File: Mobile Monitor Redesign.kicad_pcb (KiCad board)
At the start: 4 copper layers, 49 x 39.1 mm, 98 parts, among them J1 Conn_01x02_Pin, J2 Conn_01x08_Pin, J3 Conn_01x08_Pin, J4 USB_C_Receptacle_USB2.0_16P, J5 Conn_02x03_Odd_Even, J6 Micro_SD_Card_Det1, J7 Conn_01x05_Pin, J8 Conn_01x06_Socket, Q1 2N7002, Q2 AO3401A, Q5 AO3401A, Q6 2N7002, SW1 SW_Push, U1 ATmega2560-16A, U10 BQ27441DRZR-G1A, U11 TPL5010, U2 DS3232M, U5 XL4005, U6 IP5306, U7 CH340C, U8 FP6298XR, U9 AMS1117-3.3, Y1 Crystal

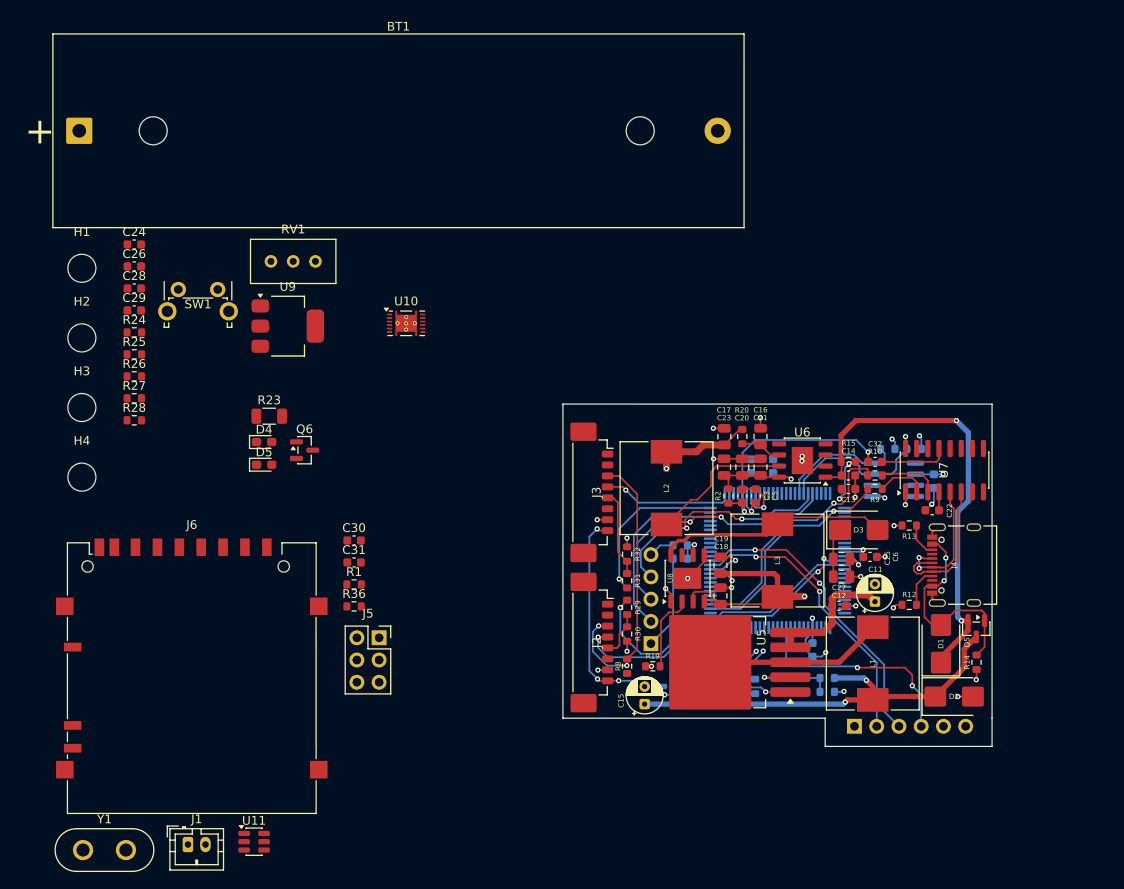
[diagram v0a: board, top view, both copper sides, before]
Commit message: cleaned up more routing and component placement
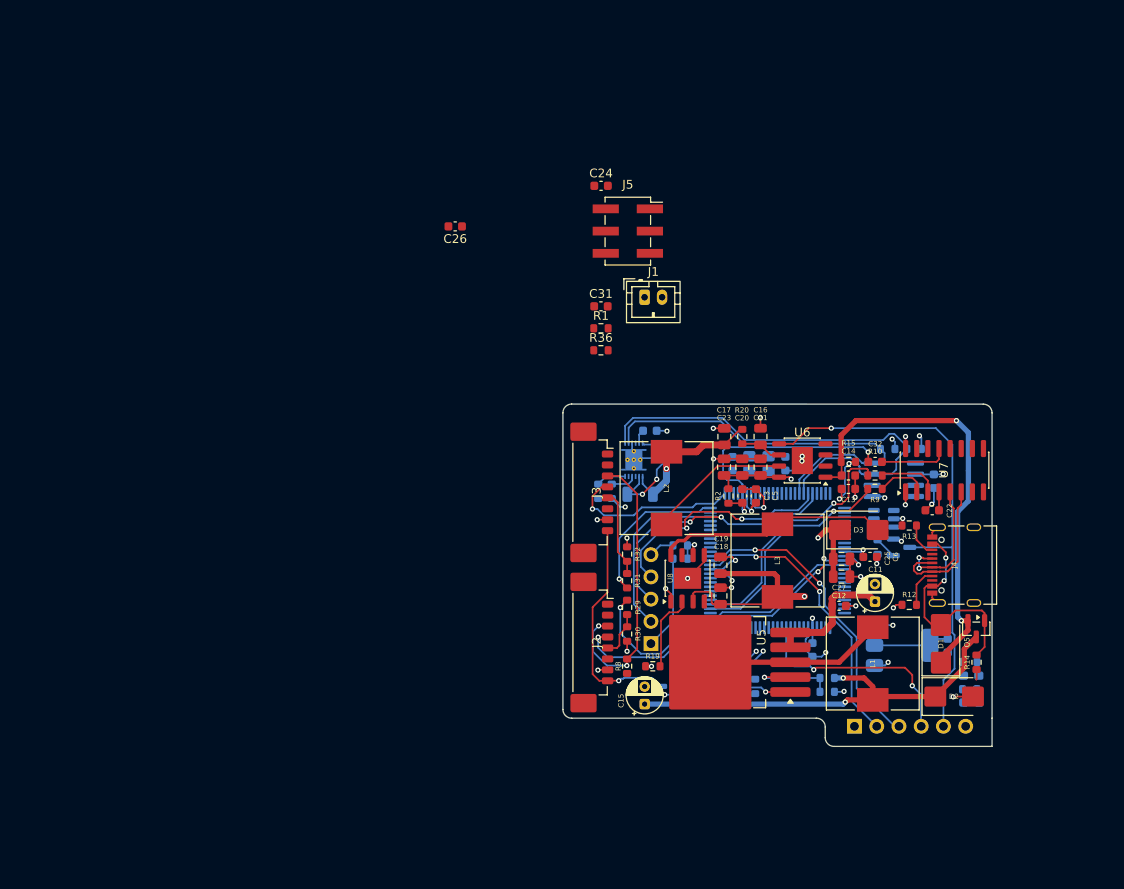
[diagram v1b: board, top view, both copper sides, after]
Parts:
- removed BT1: Battery_Cell, Battery:BatteryHolder_MPD_BH-18650-PC
- removed H1, H2, H3, H4: MountingHole, MountingHole:MountingHole_3.2mm_M3
- removed J6: Micro_SD_Card_Det1, Connector_Card:SD_Hirose_DM1AA_SF_PEJ82
- removed RV1: R_Potentiometer_Trim, Potentiometer_THT:Potentiometer_Bourns_3296W_Vertical
- removed SW1: SW_Push, Button_Switch_THT:SW_Tactile_SPST_Angled_PTS645Vx58-2LFS
- C28, C29, C30, D4, D5, Q6, R23, R24, R25, R26, R27, R28, U10, U11, U9: moved to B.Cu
- J5: footprint Connector_PinSocket_2.54mm:PinSocket_2x03_P2.54mm_Vertical -> Connector_PinSocket_2.54mm:PinSocket_2x03_P2.54mm_Vertical_SMD
- Y1: footprint Crystal:Crystal_HC50_Vertical -> Crystal:Crystal_SMD_3225-4Pin_3.2x2.5mm; moved to B.Cu
- moved R28 100.2 mm to (163.3, 113.8), turned to 180 degrees
- moved R27 100.1 mm to (163.3, 110.7)
- moved Y1 88.9 mm to (139.2, 88.0)
- moved R25 87.7 mm to (152.8, 97.5), turned to 90 degrees
- moved D5 85.2 mm to (163.5, 115.3), turned to 180 degrees
- moved D4 85.0 mm to (163.5, 112.2), turned to 180 degrees
- moved J1 81.4 mm to (126.2, 69.0)
- moved U11 80.8 mm to (153.5, 94.3), turned to 180 degrees
- moved U9 79.1 mm to (155.6, 108.8)
- moved Q6 69.1 mm to (155.5, 97.6)
- moved C30 68.8 mm to (160.8, 108.8), turned to -90 degrees
- moved C28 62.5 mm to (127.5, 86.6), turned to -90 degrees
- moved C29 60.5 mm to (126.8, 84.3)
- moved R24 57.5 mm to (122.4, 91.2), turned to 90 degrees
- moved R26 54.6 mm to (120.9, 91.2), turned to 90 degrees
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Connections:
- J8 pad 5: unconnected-(J8-Pin_5-Pad5) -> PWR_SWITCH
- R27 pad 2: status_led -> VIN
- R28 pad 1: VIN -> status_led
- U1 pad 71: unconnected-(U1-PA7-Pad71) -> status_led
- U10 pad 1: /power/SDA -> SDA
- U10 pad 2: /power/SCL -> SCL
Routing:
- net PWR_SWITCH: track 0.00 -> 59.0 mm, vias 0 -> 1
- net SDA: track 17.3 -> 54.1 mm
- net SCL: track 14.5 -> 46.7 mm
- net ADJUSTABLE_GSM_PWR_4.2: track 16.4 -> 47.4 mm, vias 0 -> 1
- net GND: track 81.0 -> 95.0 mm, vias 31 -> 34
- net /power/BATTERY_PRIMARY: track 0.00 -> 13.5 mm, vias 0 -> 2
- net +3.3V: track 0.00 -> 8.66 mm
- net /power/BATTERY_SEC: track 62.7 -> 68.8 mm
- net SOFT_PWR_SWITCH: track 0.00 -> 5.79 mm
- net PMS_RX: track 15.0 -> 20.1 mm
- net Net-(U10-GPOUT): track 0.00 -> 3.43 mm
- net RESET: track 26.2 -> 29.5 mm
- net Net-(U10-BIN): track 0.00 -> 2.95 mm
- net +5V: track 41.5 -> 43.6 mm, vias 11 -> 12
- net Net-(U10-V_{DD}): track 0.00 -> 1.54 mm
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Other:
- outline, holes or cut-outs redrawn

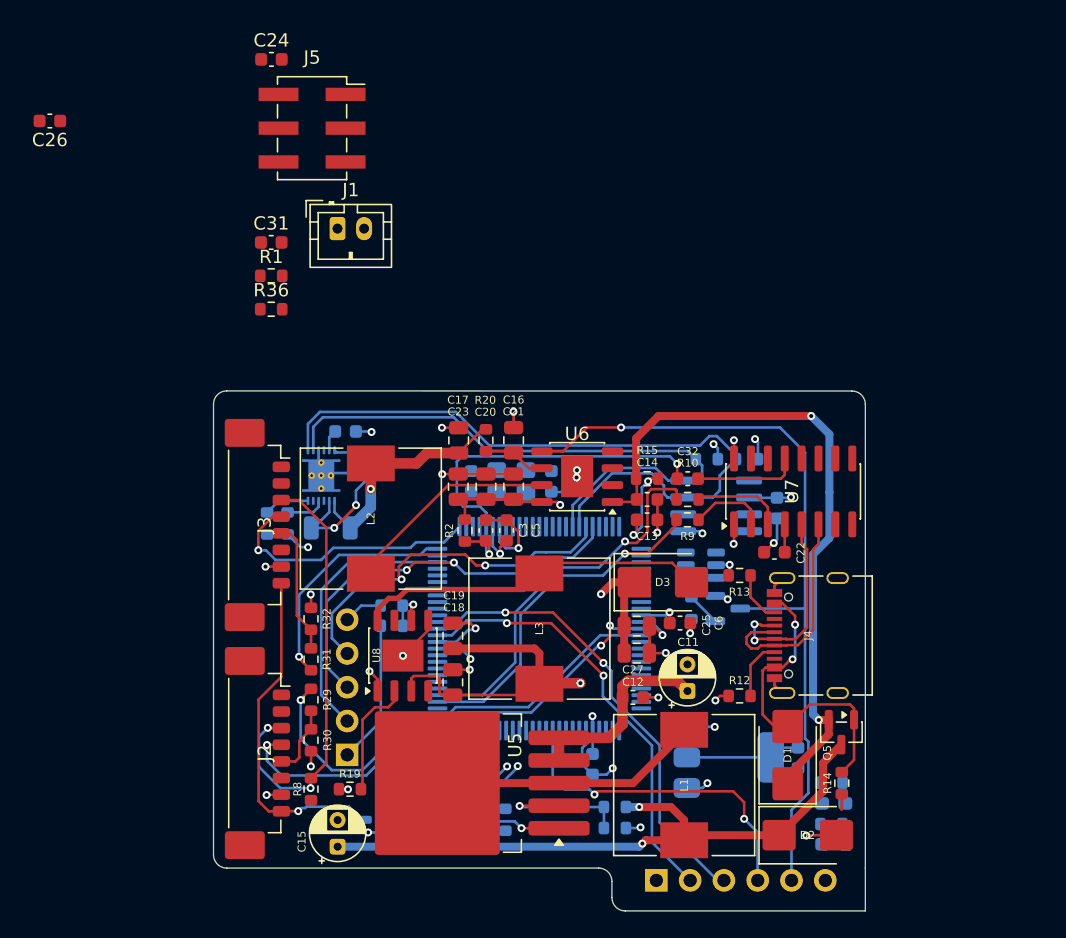
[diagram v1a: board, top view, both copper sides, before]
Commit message: routed the l80 gps daughter board and a few more modifications
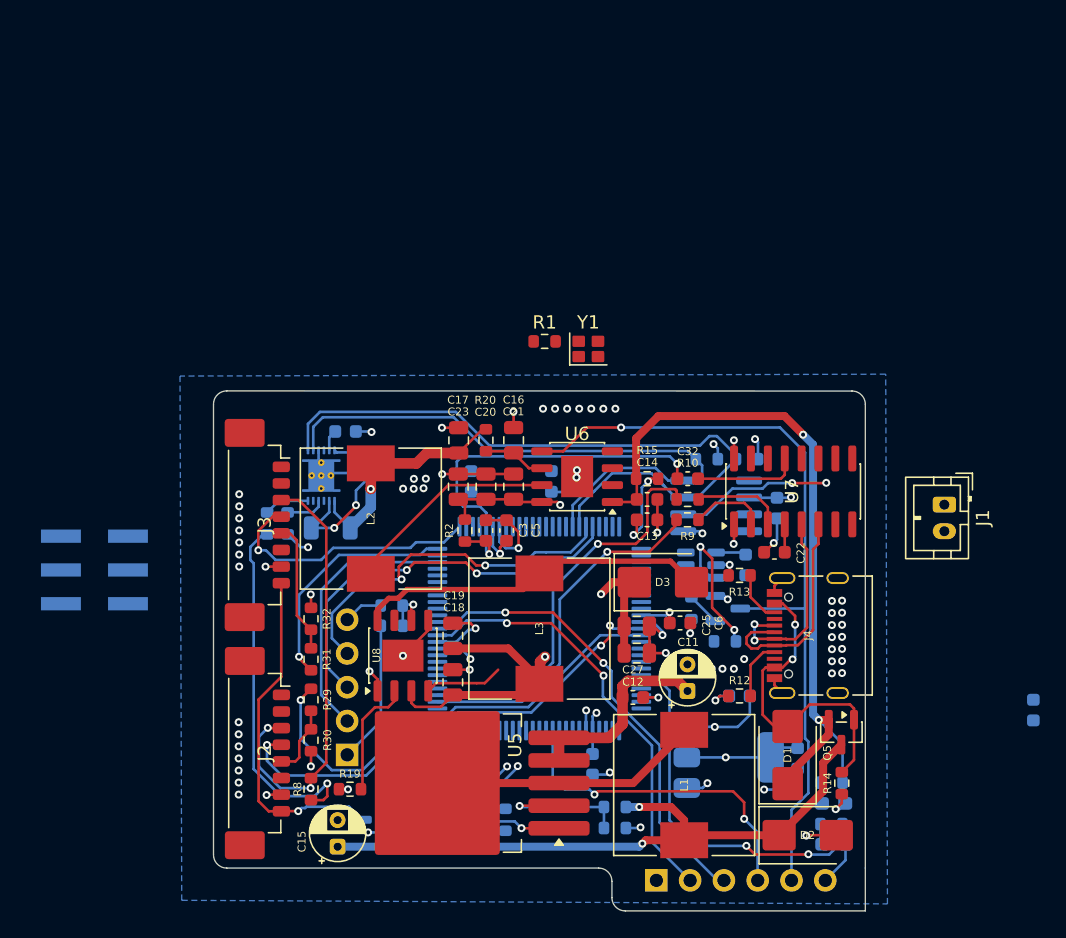
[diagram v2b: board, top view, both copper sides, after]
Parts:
- C24, C26, C31, J5, R36: moved to B.Cu
- Y1: value Crystal -> Crystal_GND23; footprint Crystal:Crystal_SMD_3225-4Pin_3.2x2.5mm -> Crystal:Crystal_SMD_SeikoEpson_FA128-4Pin_2.0x1.6mm; moved to F.Cu
- moved C26 73.9 mm to (160.8, 108.8), turned to -90 degrees
- moved C24 59.4 mm to (156.4, 104.1), turned to 180 degrees
- moved J1 50.1 mm to (171.8, 89.8), turned to -90 degrees
- moved C31 43.1 mm to (156.8, 94.3), turned to -90 degrees
- moved R36 42.3 mm to (155.3, 100.0)
- moved J5 37.0 mm to (107.9, 94.7), turned to 180 degrees
- moved R1 21.1 mm to (141.7, 77.5)
- moved C30 18.1 mm to (178.5, 105.2)
- moved Y1 11.5 mm to (145.0, 78.1)
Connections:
- Y1 pad 1: Net-(U1-XTAL2) -> Net-(U1-XTAL1)
- Y1 pad 2: Net-(U1-XTAL1) -> GND
- Y1 pad 3: (no net) -> GND
- Y1 pad 4: (no net) -> Net-(U1-XTAL2)
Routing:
- net +3.3V: track 8.66 -> 67.9 mm, vias 0 -> 2
- net status_led: track 0.00 -> 27.9 mm, vias 0 -> 2
- net VBAT_RTC: track 0.00 -> 11.7 mm, vias 0 -> 2
- net Net-(U11-DELAY/M_RST): track 0.00 -> 11.4 mm, vias 0 -> 2
- net GND: track 95.0 -> 101.5 mm, vias 34 -> 81
- net GSM_PWR_EN: track 0.00 -> 5.92 mm
- net +5V: track 43.6 -> 48.4 mm
- net /power/BATTERY_SEC: track 68.8 -> 64.7 mm
- net VIN: track 51.3 -> 54.6 mm
- net /BATTERY_SEC: track 0.00 -> 2.29 mm
- net ADJUSTABLE_GSM_PWR_4.2: track 47.4 -> 45.3 mm
- net Net-(D4-A): track 0.00 -> 1.60 mm
- net Net-(D5-A): track 0.00 -> 1.58 mm
- net TXD0: track 29.1 -> 30.1 mm
- net RXD0: track 26.1 -> 26.7 mm
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- added copper zone on B.Cu, net GND

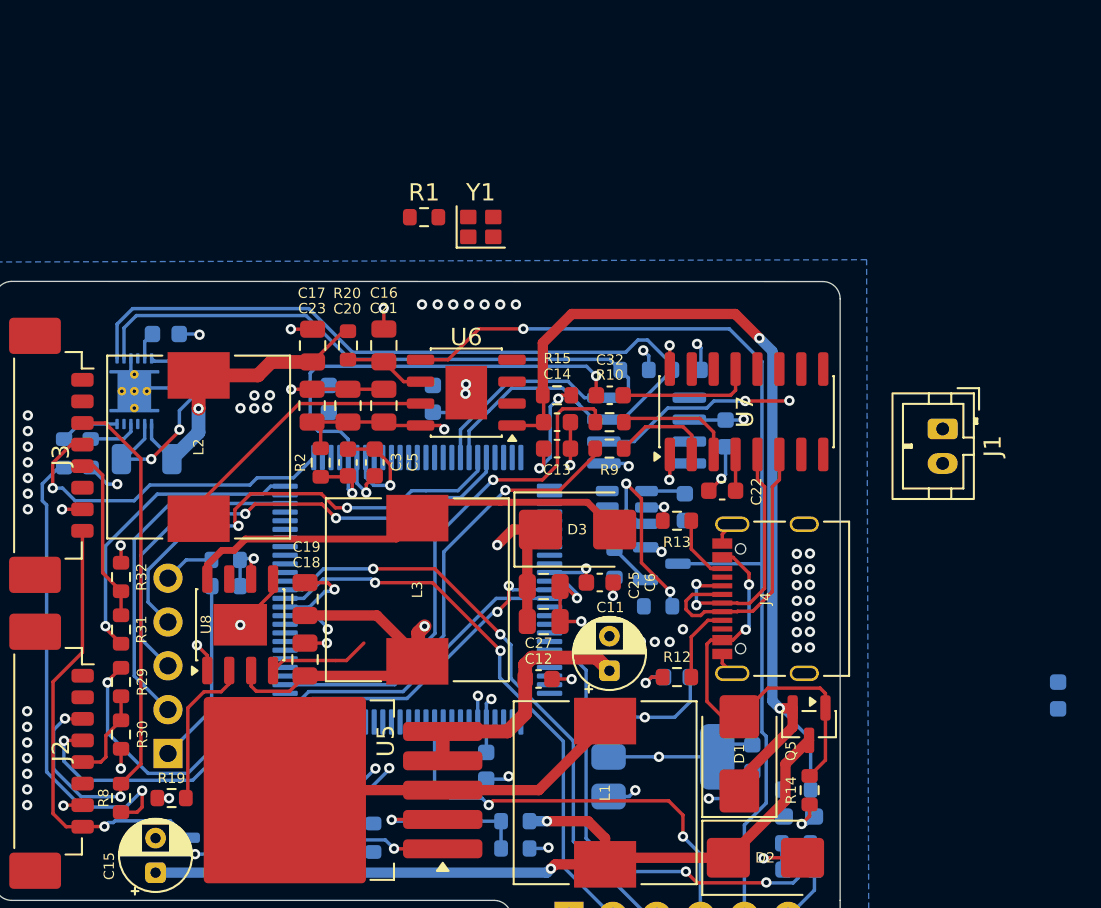
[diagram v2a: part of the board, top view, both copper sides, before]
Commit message: updated routing and placement of devices on both PCBS
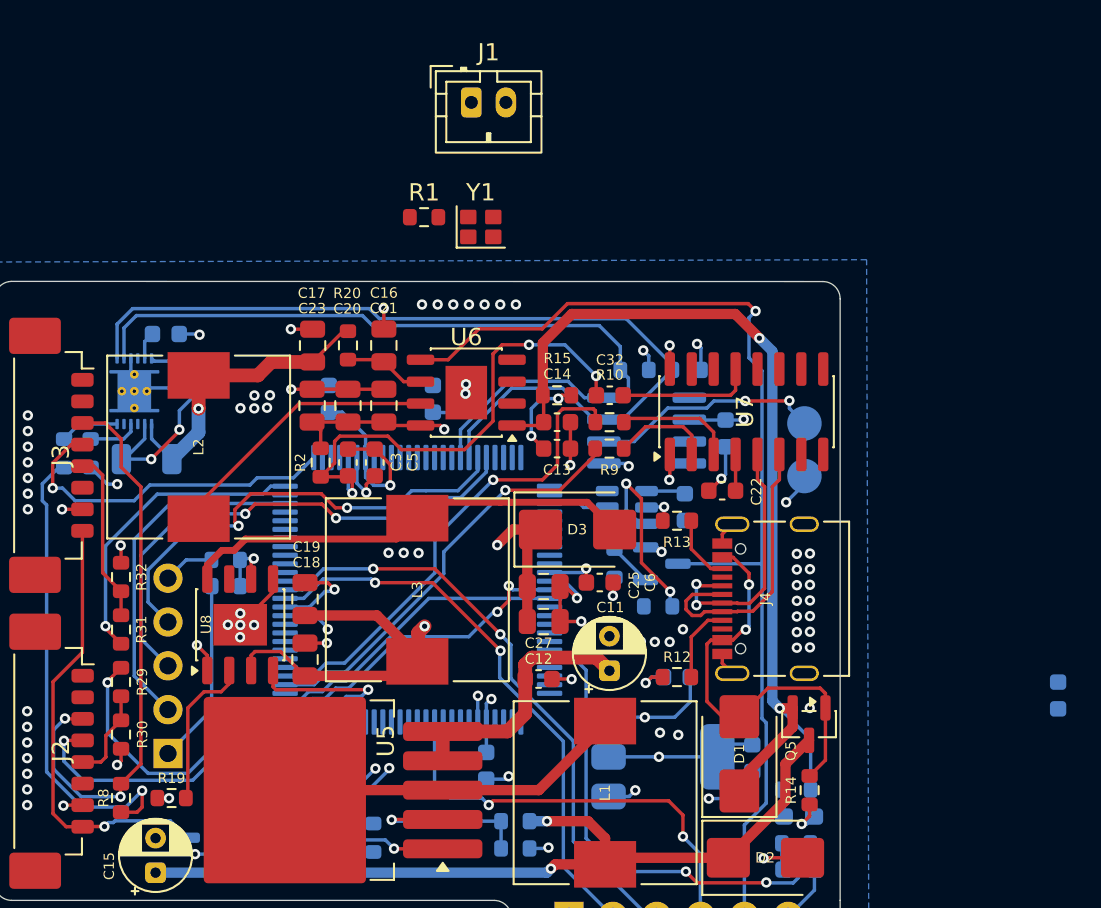
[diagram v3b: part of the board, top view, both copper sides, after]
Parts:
- added REF**: TestPoint_Pad_D2.0mm, TestPoint:TestPoint_Pad_D2.0mm, B.Cu at (163.8, 89.4)
- added REF**: TestPoint_Pad_D2.0mm, TestPoint:TestPoint_Pad_D2.0mm, B.Cu at (163.8, 92.5)
- moved J1 33.2 mm to (144.5, 70.8), turned to 0 degrees
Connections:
- U1 pad 53: unconnected-(U1-PC0-Pad53) -> SOFT_PWR_SWITCH
- U1 pad 97: unconnected-(U1-PF0-Pad97) -> GSM_PWR_EN
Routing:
- net GND: track 101.5 -> 107.3 mm, vias 81 -> 92
- net GSM_PWR_EN: track 5.92 -> 9.59 mm, vias 0 -> 1
- net SOFT_PWR_SWITCH: track 5.79 -> 9.23 mm
- net PWR_SWITCH: track 59.0 -> 62.0 mm
- net RXD0: track 26.7 -> 24.6 mm
- net TXD0: track 30.1 -> 28.0 mm
- net VBAT_RTC: track 11.7 -> 13.4 mm
- net Net-(C13-Pad1): track 6.57 -> 5.25 mm
- net SDA: track 53.5 -> 52.5 mm
- net SCL: track 46.7 -> 47.5 mm
- net RESET: vias 2 -> 3
